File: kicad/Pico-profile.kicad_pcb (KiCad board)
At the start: 2 copper layers, 124 x 79 mm, 42 parts, among them J1 Parallel, J2 DB25_Female, J3 Micro_SD_Card, J4 I2C, J5 Screw_Terminal_01x02, U1 74LS280, U2 74LS244, U3 74LVC244, U4 74LVC2G240, U5 74LVC1G04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

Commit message: Added gerbers for prototype production
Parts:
- added G***: LOGO, logos:lisa_logo, F.Cu at (216.8, 106.5)
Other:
- board text added: "SD card"
- board text added: "https://github.com/BwanaFr/pico-profile"
- board text added: "v1.0.0"

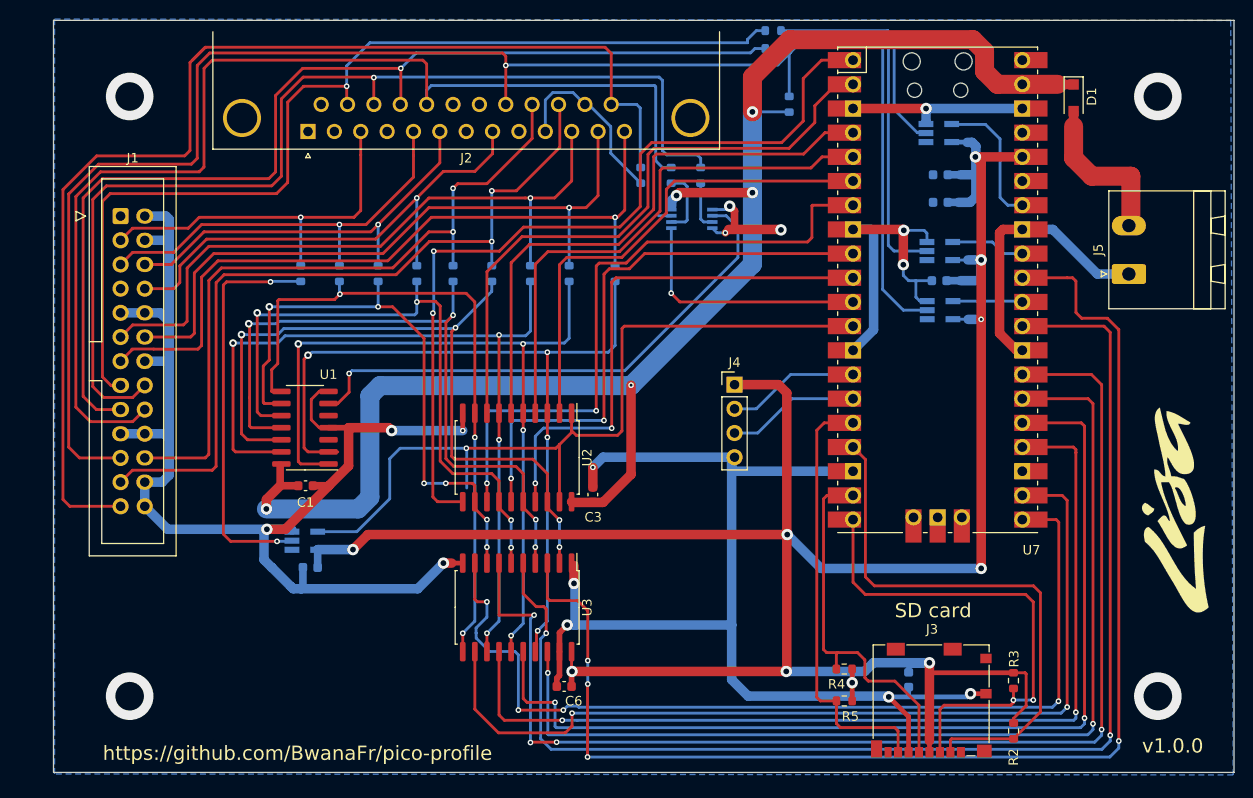
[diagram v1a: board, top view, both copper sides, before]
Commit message: Fixed PCB footprint. Added more silkscreen information.
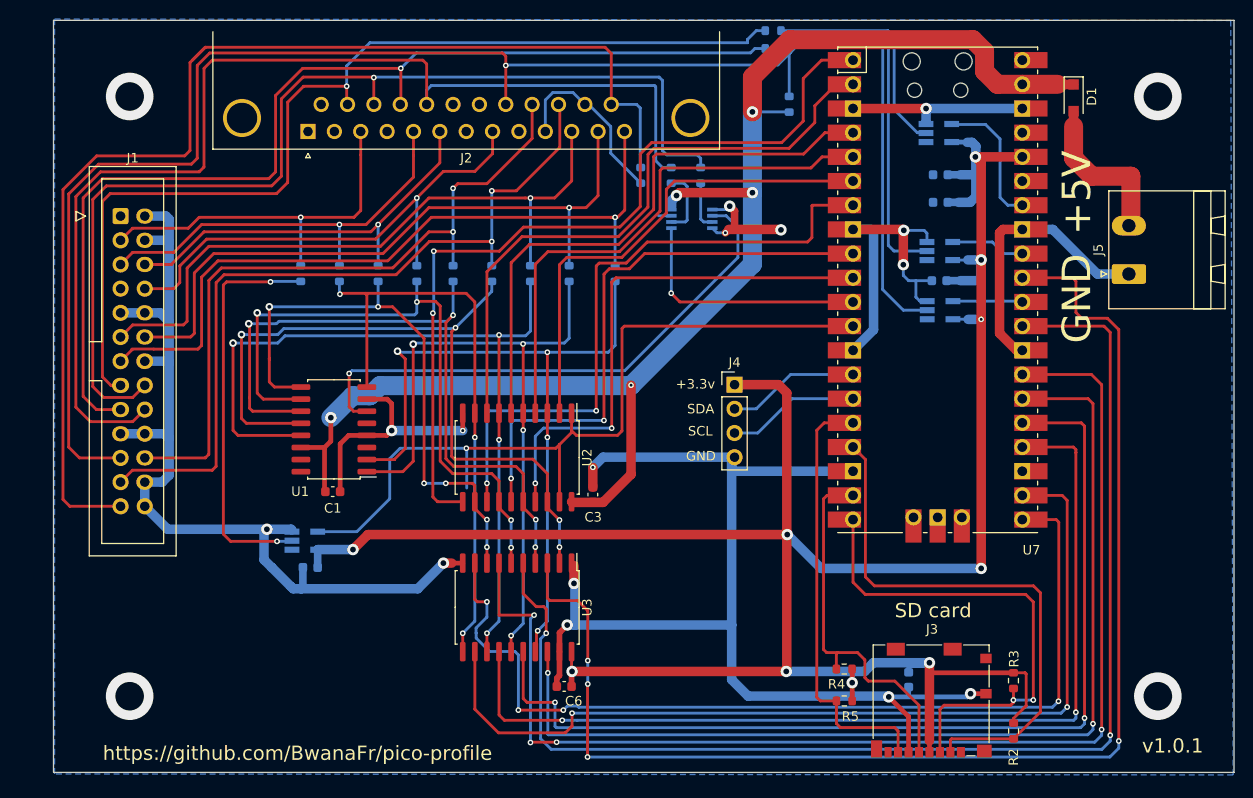
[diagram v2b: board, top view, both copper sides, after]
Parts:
- removed G***: LOGO, logos:lisa_logo
- R2: value 47k -> 4.7k
- U1: footprint Package_SO:SO-14_3.9x8.65mm_P1.27mm -> Package_SO:SO-16_5.3x10.2mm_P1.27mm
- moved U1 3.05 mm to (128.5, 98.0)
- moved C1 2.92 mm to (128.3, 104.5)
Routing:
- net GND: track 374.7 -> 361.1 mm
- net +5VL: track 163.4 -> 149.9 mm
- net /PD6: track 83.2 -> 73.2 mm
- net /PD7: track 85.3 -> 77.4 mm
- net /PD0: track 70.9 -> 63.0 mm
- net Net-(U1-Pad6): track 56.9 -> 57.8 mm
- net /PD1: track 61.9 -> 61.3 mm
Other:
- board text added: "+3.3v"
- board text added: "+5V"
- board text added: "GND"
- board text added: "SCL"
- board text added: "SDA"
- board text added: "v1.0.1"
- board text removed: "v1.0.0"
